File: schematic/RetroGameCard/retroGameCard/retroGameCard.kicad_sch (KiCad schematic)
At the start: 34 parts, among them IC1 STM32C562KET6, J1 Conn_01x04_Pin, J2 Conn_01x04_Pin, J3 USB_C_Receptacle_USB2.0_16P, SW1 SW_Slide_DPDT, SW2 SW_SPDT, SW3 SW_Push, SW4 SW_Push, SW5 SW_Push, SW6 SW_Push, SW7 SW_Push, U1 MCP73831-2-OT, U2 AP2112K-3.3

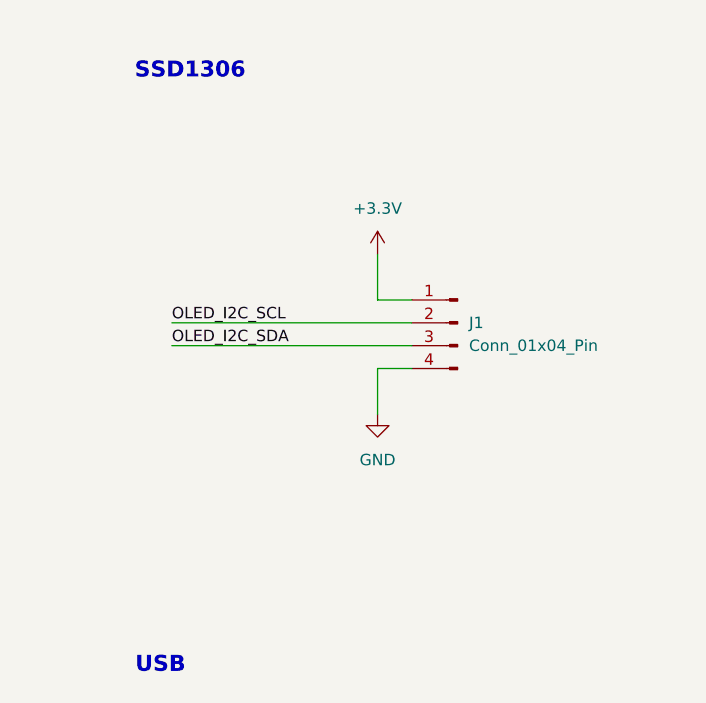
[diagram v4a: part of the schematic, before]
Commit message: added footprints to symbols
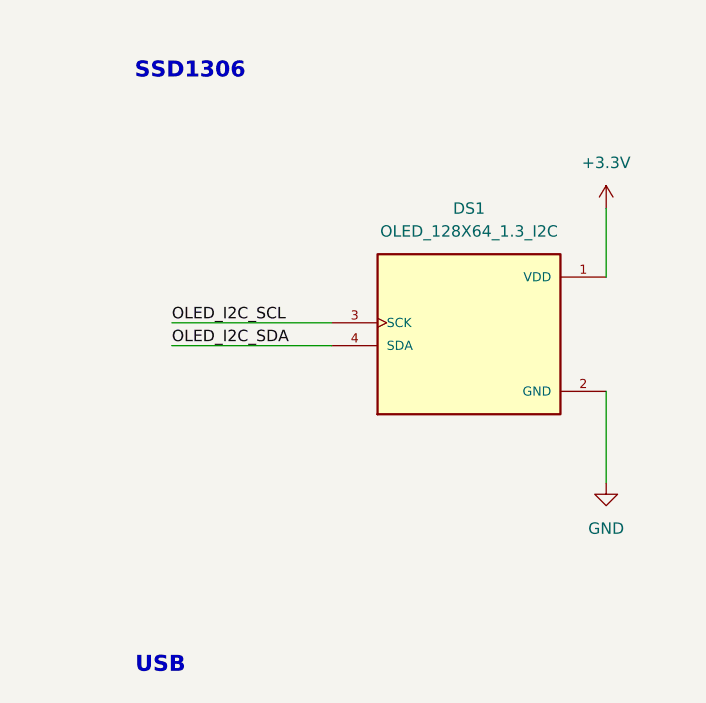
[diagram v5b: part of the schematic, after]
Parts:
- removed J1: Conn_01x04_Pin, symbol Connector:Conn_01x04_Pin
- added DS1: OLED_128X64_1.3_I2C, OLED_128X64_1.3_I2C:LCD_OLED_128X64_1.3_I2C, symbol OLED_128X64_1.3_I2C:OLED_128X64_1.3_I2C
- C1, C10, C2, C3, C4, C6, C7, C8, C9: footprint (none) -> Capacitor_SMD:C_0805_2012Metric_Pad1.18x1.45mm_HandSolder
- C11: footprint (none) -> Connector_JST:JST_EH_S2B-EH_1x02_P2.50mm_Horizontal
- C5: footprint (none) -> Capacitor_SMD:C_1206_3216Metric_Pad1.33x1.80mm_HandSolder
- D1, D2: footprint (none) -> LED_SMD:LED_0805_2012Metric_Pad1.15x1.40mm_HandSolder
- J2: footprint (none) -> Connector_JST:JST_EH_B4B-EH-A_1x04_P2.50mm_Vertical
- J3: footprint (none) -> Connector_USB:USB_C_Receptacle_GCT_USB4085
- R1, R2, R3, R4, R5, R6, R7, R8: footprint (none) -> Resistor_SMD:R_0805_2012Metric_Pad1.20x1.40mm_HandSolder
- SW1, SW2: footprint (none) -> Button_Switch_THT:SW_Slide-03_Wuerth-WS-SLTV_10x2.5x6.4_P2.54mm
- SW3, SW4, SW5, SW6, SW7: footprint (none) -> Button_Switch_THT:SW_PUSH_6mm
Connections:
- net +3.3V: now also DS1.1 (VDD)
- net GND: now also DS1.2 (GND)
- net OLED_I2C_SCL: now also DS1.3 (SCK)
- net OLED_I2C_SDA: now also DS1.4 (SDA)

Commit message: changed shemat footprints
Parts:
- J3: footprint Connector_USB:USB_C_Receptacle_GCT_USB4085 -> Connector_USB:USB_C_Receptacle_GCT_USB4110
- SW1, SW2: footprint Button_Switch_THT:SW_Slide-03_Wuerth-WS-SLTV_10x2.5x6.4_P2.54mm -> Button_Switch_SMD:SW_SPDT_PCM12
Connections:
- net OLED_I2C_SCL: now also IC1.29 (PB6); no longer IC1.19 (PA8)
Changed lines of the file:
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@@
 	)
 	(junction
-		(at 105.41 179.07)
-		(diameter 0)
-		(color 0 0 0 0)
-	)
-	(junction
 		(at 25.4 33.02)
 		(diameter 0)
@@
 	)
 	(no_connect
-		(at 78.74 157.48)
-	)
-	(no_connect
 		(at 121.92 162.56)
 	)
@@
 	)
 	(no_connect
+		(at 121.92 147.32)
+	)
+	(no_connect
 		(at 78.74 154.94)
 	)
@@
 	(wire
 		(pts
-			(xy 105.41 180.34) (xy 105.41 179.07)
-		)
-		(stroke
-			(width 0)
-			(type default)
-		)
-	)
-	(wire
-		(pts
 			(xy 179.07 143.51) (xy 190.5 143.51)
 		)
@@
 	(wire
 		(pts
-			(xy 121.92 147.32) (xy 139.7 147.32)
-		)
-		(stroke
-			(width 0)
-			(type default)
-		)
-	)
-	(wire
-		(pts
 			(xy 40.64 127) (xy 43.18 127)
 		)
@@
 	(wire
 		(pts
-			(xy 105.41 179.07) (xy 124.46 179.07)
-		)
-		(stroke
-			(width 0)
-			(type default)
-		)
-	)
-	(wire
-		(pts
 			(xy 165.1 168.91) (xy 165.1 170.18)
 		)
@@
 	(wire
 		(pts
-			(xy 105.41 179.07) (xy 105.41 177.8)
+			(xy 105.41 177.8) (xy 105.41 180.34)
 		)
 		(stroke
@@
 	(wire
 		(pts
+			(xy 60.96 157.48) (xy 78.74 157.48)
+		)
+		(stroke
+			(width 0)
+			(type default)
+		)
+	)
+	(wire
+		(pts
 			(xy 160.02 168.91) (xy 160.02 177.8)
 		)
@@
 		)
 	)
+	(label "OLED_I2C_SCL"
+		(at 60.96 157.48 0)
+		(effects
+			(font
+				(size 1.27 1.27)
+			)
+			(justify left bottom)
+		)
+	)
 	(label "Vbat"
 		(at 99.06 35.56 0)
@@
 		)
 	)
-	(label "OLED_I2C_SCL"
-		(at 139.7 147.32 180)
-		(effects
-			(font
-				(size 1.27 1.27)
-			)
-			(justify right bottom)
-		)
-	)
 	(label "LEFT"
 		(at 158.75 129.54 0)
@@
 	)
 	(symbol
-		(lib_id "power:PWR_FLAG")
-		(at 124.46 179.07 0)
-		(unit 1)
-		(body_style 1)
-		(exclude_from_sim no)
-		(in_bom yes)
-		(on_board yes)
-		(in_pos_files yes)
-		(dnp no)
-		(fields_autoplaced yes)
-		(property "Reference" "#FLG05"
-			(at 124.46 177.165 0)
-			(hide yes)
-			(show_name no)
-			(do_not_autoplace no)
-			(effects
-				(font
-					(size 1.27 1.27)
-				)
-			)
-		)
-		(property "Value" "PWR_FLAG"
-			(at 124.46 173.99 0)
-			(show_name no)
-			(do_not_autoplace no)
-			(effects
-				(font
-					(size 1.27 1.27)
-				)
-			)
-		)
-		(property "Footprint" ""
-			(at 124.46 179.07 0)
-			(hide yes)
-			(show_name no)
-			(do_not_autoplace no)
-			(effects
-				(font
-					(size 1.27 1.27)
-				)
-			)
-		)
-		(property "Datasheet" ""
-			(at 124.46 179.07 0)
-			(hide yes)
-			(show_name no)
-			(do_not_autoplace no)
-			(effects
-				(font
-					(size 1.27 1.27)
-				)
-			)
-		)
-		(property "Description" "Special symbol for telling ERC where power comes from"
-			(at 124.46 179.07 0)
-			(hide yes)
-			(show_name no)
-			(do_not_autoplace no)
-			(effects
-				(font
-					(size 1.27 1.27)
-				)
-			)
-		)
-		(pin "1"
-		)
-		(instances
-			(project "retroGameCard"
-				(path "/de252b9d-dba4-4c47-b073-f66cc96c1065"
-					(reference "#FLG05")
-					(unit 1)
-				)
-			)
-		)
-	)
-	(symbol
 		(lib_id "power:+3.3V")
 		(at 105.41 97.79 0)
@@
 			)
 		)
-		(property "Footprint" "Button_Switch_THT:SW_Slide-03_Wuerth-WS-SLTV_10x2.5x6.4_P2.54mm"
+		(property "Footprint" "Button_Switch_SMD:SW_SPDT_PCM12"
 			(at 151.13 41.91 0)
 			(hide yes)
@@
 			)
 		)
-		(property "Footprint" "Connector_USB:USB_C_Receptacle_GCT_USB4085"
+		(property "Footprint" "Connector_USB:USB_C_Receptacle_GCT_USB4110"
 			(at 246.38 118.11 0)
 			(hide yes)
@@
 			)
 		)
-		(property "Footprint" "Button_Switch_THT:SW_Slide-03_Wuerth-WS-SLTV_10x2.5x6.4_P2.54mm"
+		(property "Footprint" "Button_Switch_SMD:SW_SPDT_PCM12"
 			(at 48.26 129.54 0)
 			(hide yes)

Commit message: changed footprints and oled
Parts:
- removed DS1: OLED_128X64_1.3_I2C, OLED_128X64_1.3_I2C:LCD_OLED_128X64_1.3_I2C, symbol OLED_128X64_1.3_I2C:OLED_128X64_1.3_I2C
- added U3: DM-OLED096-636, OLED_128x64_0.96_I2C:MODULE_DM-OLED096-636, symbol OLED_096x64_I2C:DM-OLED096-636
- C11: footprint Connector_JST:JST_EH_S2B-EH_1x02_P2.50mm_Horizontal -> TestPoint:Bez_nazwy_1
- J2: footprint Connector_JST:JST_EH_B4B-EH-A_1x04_P2.50mm_Vertical -> Connector_PinHeader_2.54mm:PinHeader_1x04_P2.54mm_Horizontal
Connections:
- net +3.3V: now also U3.2 (VCC_IN)
- net GND: now also U3.1 (GND)
- net OLED_I2C_SCL: now also U3.3 (SCL)
- net OLED_I2C_SDA: now also U3.4 (SDA)
- net SWCLK: now also J2.2 (Pin_2); no longer J2.3 (Pin_3)
- net SWDIO: now also J2.3 (Pin_3); no longer J2.2 (Pin_2)

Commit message: update schematic
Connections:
- net LEFT: now also IC1.12 (PA6); no longer IC1.9 (PA3)
- net RIGHT: now also IC1.9 (PA3); no longer IC1.13 (PA7)
- net UP: now also IC1.13 (PA7); no longer IC1.12 (PA6)
- net at IC1.14 (PB0): no longer D2.2 (A)
- net LED: now reaches IC1.8 (PA2)
- net LED: now also D2.2 (A)
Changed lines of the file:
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@@
+	)
+	(no_connect
+		(at 78.74 147.32)
 	)
 	(no_connect
@@
 		(at 132.08 52.07)
 	)
-	(no_connect
-		(at 121.92 132.08)
-	)
 	(wire
 		(pts
@@
 	(wire
 		(pts
+			(xy 121.92 132.08) (xy 128.27 132.08)
+		)
+		(stroke
+			(width 0)
+			(type default)
+		)
+	)
+	(wire
+		(pts
 			(xy 250.19 140.97) (xy 250.19 144.78)
 		)
@@
 	(wire
 		(pts
+			(xy 50.8 144.78) (xy 50.8 147.32)
+		)
+		(stroke
+			(width 0)
+			(type default)
+		)
+	)
+	(wire
+		(pts
 			(xy 160.02 177.8) (xy 165.1 177.8)
 		)
@@
 		(pts
 			(xy 40.64 44.45) (xy 40.64 48.26)
-		)
-		(stroke
-			(width 0)
-			(type default)
-		)
-	)
-	(wire
-		(pts
-			(xy 50.8 147.32) (xy 78.74 147.32)
 		)
 		(stroke
@@
 		)
 	)
-	(label "LEFT"
+	(label "RIGHT"
 		(at 139.7 134.62 180)
 		(effects
@@
 		)
 	)
-	(label "UP"
+	(label "LEFT"
 		(at 139.7 142.24 180)
 		(effects
@@
 		)
 	)
+	(label "LED"
+		(at 128.27 132.08 180)
+		(effects
+			(font
+				(size 1.27 1.27)
+			)
+			(justify right bottom)
+		)
+	)
+	(label "LED"
+		(at 50.8 144.78 0)
+		(effects
+			(font
+				(size 1.27 1.27)
+			)
+			(justify left bottom)
+		)
+	)
 	(label "SWCLK"
 		(at 160.02 102.87 0)
@@
 		)
 	)
-	(label "RIGHT"
+	(label "UP"
 		(at 139.7 144.78 180)
 		(effects
